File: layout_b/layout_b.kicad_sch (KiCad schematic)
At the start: 37 parts, among them J1 platform UART, J10 Conn_01x08, J3 CSI2 Camera, J4 Lidar, J5 MSD-4-A, J6 Power, Q1 TSM500P02CX_RFG, SW1 RST, U1 MLX90614ESF-BAA-000-TU, U3 BNO085, U5 ESP32-P4_MODULE

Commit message: layout b updated
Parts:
- added H1, H2, H3, H4: MountingHole, MountingHole:MountingHole_3.2mm_M3, symbol Mechanical:MountingHole
- added J11: TSM-113-01-L-DH-A-P-TR, Library:SAMTEC_TSM-113-01-L-DH-A-P-TR, symbol Library:TSM-113-01-L-DH-A-P-TR
- added J7: Radar UART, Connector_JST:JST_EH_B2B-EH-A_1x02_P2.50mm_Vertical, symbol Connector_Generic:Conn_01x02
- SW1: footprint Button_Switch_SMD:SW_Push_1P1T_XKB_TS-1187A -> Button_Switch_SMD:SW_SPST_CK_RS282G05A3
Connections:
- net +3V3: now also J11.01
- net +5V: now also J11.02
- net CD: now also U5.25 (GPIO10); no longer U5.29 (GPIO20)
- net COVER_GND: now also J11.25, J11.26
- net D0: now also U5.23 (GPIO8); no longer U5.27 (GPIO12)
- net D1: now also U5.24 (GPIO9); no longer U5.28 (GPIO13)
- net D2: now also U5.20 (GPIO5); no longer U5.23 (GPIO8)
- net D3: now also U5.19 (GPIO4); no longer U5.24 (GPIO9)
- net SDCLK: now also U5.17 (GPIO2); no longer U5.26 (GPIO11)
- net SDCMD: now also U5.18 (GPIO3); no longer U5.25 (GPIO10)
- net RRX: now reaches U5.30 (GPIO21)
- net RRX: now also J7.2 (Pin_2)
- net RTX: now reaches U5.31 (GPIO22)
- net RTX: now also J7.1 (Pin_1)
- net 23: now reaches U5.32 (GPIO23)
- net 29: now reaches U5.56 (GPIO29)
- net 29: now also J11.20
- net 30: now reaches U5.57 (GPIO30)
- net 30: now also J11.19
- net 31: now reaches U5.58 (GPIO31)
- net 31: now also J11.18
- net 32: now reaches U5.59 (GPIO32)
- net 32: now also J11.17
- net 33: now reaches U5.60 (GPIO33)
- net 33: now also J11.16
- net 39: now reaches U5.67 (GPIO39)
- net 40: now reaches U5.68 (GPIO40)
- net 40: now also J11.15
- net 41: now reaches U5.69 (GPIO41)
- net 41: now also J11.14
- net 42: now reaches U5.70 (GPIO42)
- net 42: now also J11.13
- net 43: now reaches U5.71 (GPIO43)
- net 43: now also J11.12
- net 44: now reaches U5.72 (GPIO44)
- net 44: now also J11.11
- net 45: now reaches U5.73 (GPIO45)
- net 45: now also J11.10
- net 46: now reaches U5.74 (GPIO46)
- net 46: now also J11.09
- net 47: now reaches U5.75 (GPIO47)
- net 47: now also J11.08
- net 48: now reaches U5.76 (GPIO48)
- net 48: now also J11.07
- net 49: now reaches U5.77 (GPIO49)
- net 49: now also J11.06
- net 52: now reaches U5.80 (GPIO52)
- net 52: now also J11.05
- net 53: now reaches U5.81 (GPIO53)
- net 53: now also J11.03
- net 54: now reaches U5.82 (GPIO54)
- net 54: now also J11.04
- new net 11: J11.24, U5.26 (GPIO11)
- new net 12: J11.23, U5.27 (GPIO12)
- new net 13: J11.22, U5.28 (GPIO13)
- new net 20: J11.21, U5.29 (GPIO20)
- no-connect marks 23 -> 26
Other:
- note added: "23 spare"
- note added: "Strapping"
- moved on the sheet: J4

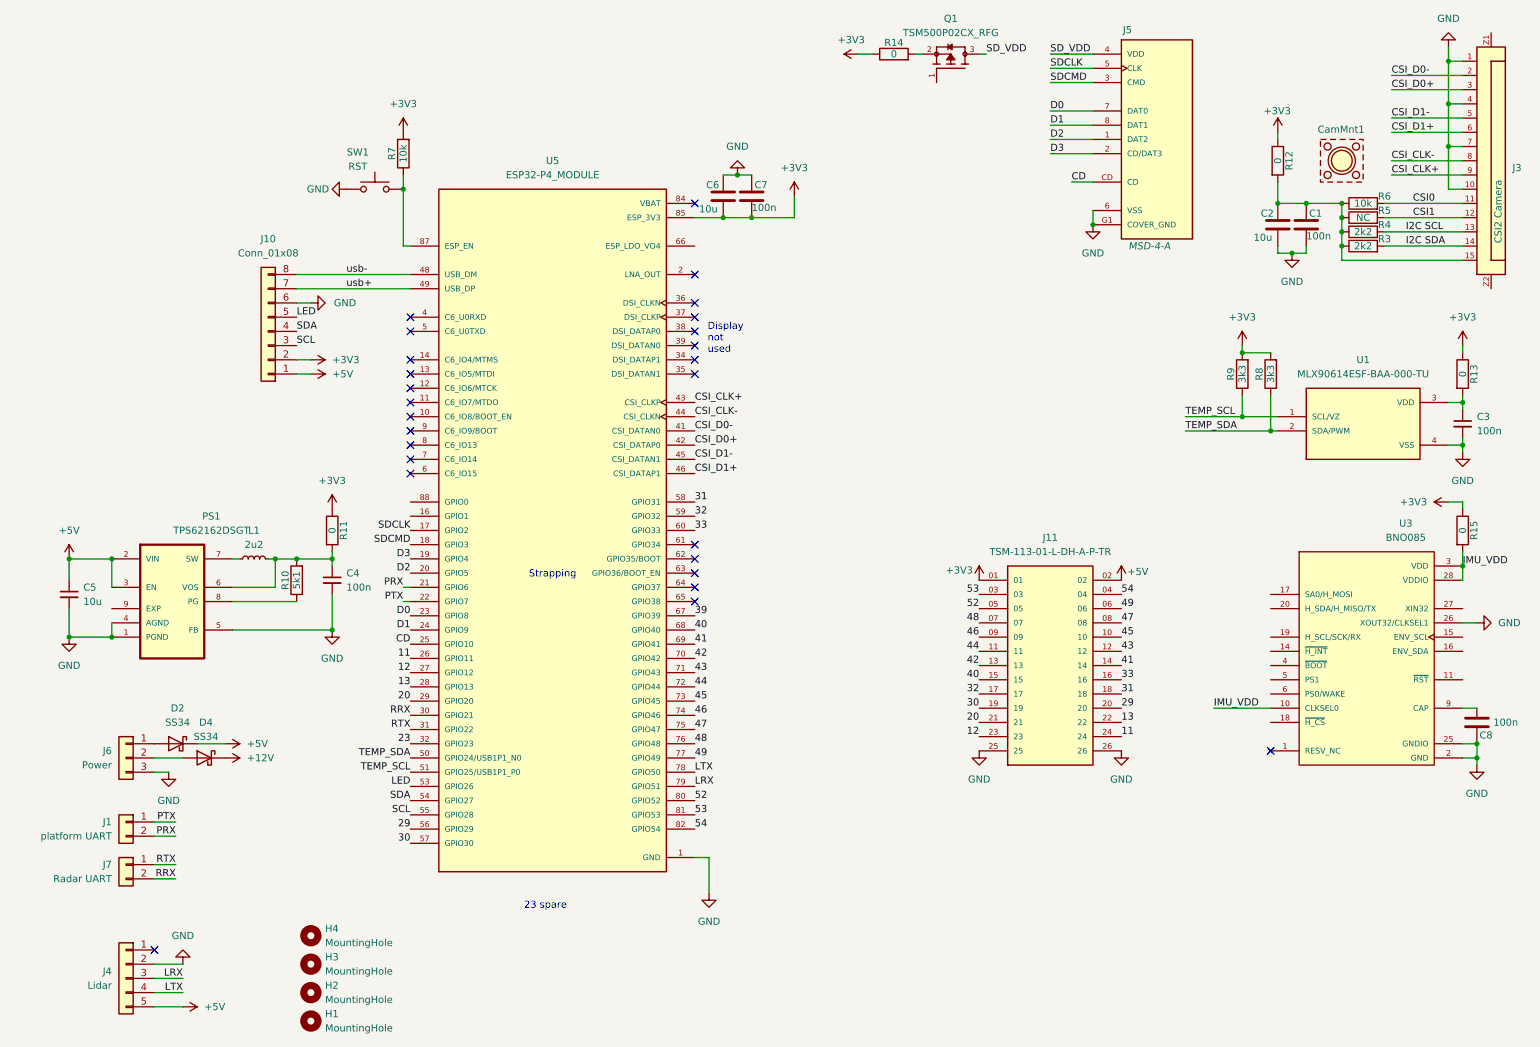
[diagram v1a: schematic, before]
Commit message: Update
added stepper driver
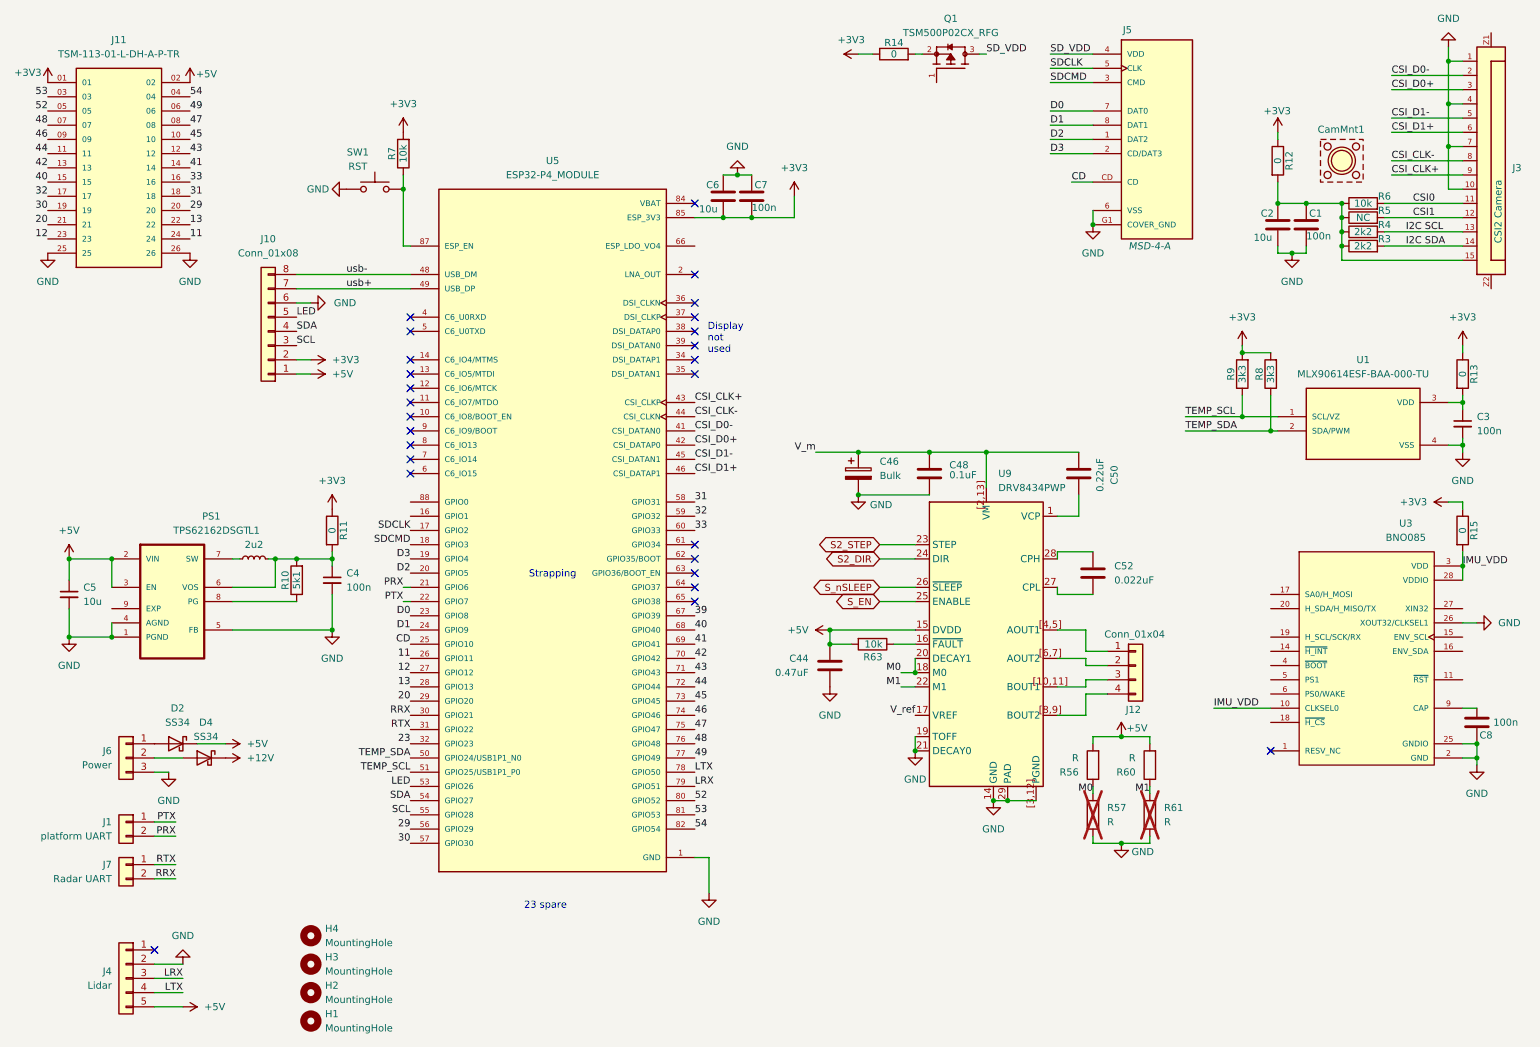
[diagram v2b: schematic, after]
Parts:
- added C44: 0.47uF, Capacitor_SMD:C_0402_1005Metric, symbol Device:C
- added C46: Bulk, Capacitor_Tantalum_SMD:CP_EIA-6032-15_Kemet-U, symbol Device:C_Polarized
- added C48: 0.1uF, Capacitor_SMD:C_0402_1005Metric, symbol Device:C
- added C50: 0.22uF, Capacitor_SMD:C_0402_1005Metric, symbol Device:C
- added C52: 0.022uF, Capacitor_SMD:C_0402_1005Metric, symbol Device:C
- added J12: Conn_01x04, Connector_JST:JST_XH_B4B-XH-A_1x04_P2.50mm_Vertical, symbol Connector_Generic:Conn_01x04
- added R56, R57, R60, R61: R, Resistor_SMD:R_0603_1608Metric, symbol Device:R
- added R63: 10k, Resistor_SMD:R_0603_1608Metric, symbol Device:R
- added U9: DRV8434PWP, Package_SO:TSSOP-28-1EP_4.4x9.7mm_P0.65mm_EP3.4x9.7mm_Mask3.1x4.05mm, symbol NEXUS:DRV8434PWP
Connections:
- net +5V: now also C44.1, R56.2, R60.2, R63.2, U9.15 (DVDD)
- net COVER_GND: now also C44.2, C46.2, C48.2, R57.2, R61.2, U9.14 (GND), U9.19 (TOFF), U9.21 (DECAY0), U9.29 (PAD), U9.[3,12] (PGND)
- new net: C50.2, U9.1 (VCP)
- new net: R63.1, U9.16 (~{FAULT})
- new net: C52.2, U9.27 (CPL)
- new net: C52.1, U9.28 (CPH)
- new net: J12.3 (Pin_3), U9.[10,11] (BOUT1)
- new net: J12.1 (Pin_1), U9.[4,5] (AOUT1)
- new net: J12.2 (Pin_2), U9.[6,7] (AOUT2)
- new net: J12.4 (Pin_4), U9.[8,9] (BOUT2)
- new net M0: R56.1, R57.1, U9.18 (M0), U9.20 (DECAY1)
- new net M1: R60.1, R61.1, U9.22 (M1)
- new net S2_DIR: U9.24 (DIR)
- new net S2_STEP: U9.23 (STEP)
- new net S_EN: U9.25 (ENABLE)
- new net S_nSLEEP: U9.26 (~{SLEEP})
- new net V_m: C46.1, C48.1, C50.1, U9.[2,13] (VM)
- new net V_ref: U9.17 (VREF)
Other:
- moved on the sheet: J11
